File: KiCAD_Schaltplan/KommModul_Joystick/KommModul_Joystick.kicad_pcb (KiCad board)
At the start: 2 copper layers, 100 x 120 mm, 46 parts, among them J1 66100411622, J2 618015231121, J3 691242510004, J4 691242510004, J5 612020235121, J6 696106003002, SW1 430182080816, SW3 472123010111, U1 STM32F303RETx, U2 SP3485EN, U3 SP3485EN, U4 TLV1117LV33DCYR, Y1 16 MHz

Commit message: PCB Routing V1
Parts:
- moved J3 85.8 mm to (95.0, 129.5), turned to 180 degrees
- moved D5 82.8 mm to (113.0, 126.0), turned to 90 degrees
- moved J4 67.8 mm to (165.0, 129.5), turned to 180 degrees
- moved D6 65.5 mm to (147.5, 126.0), turned to 90 degrees
- moved J1 65.1 mm to (143.9, 39.0)
- moved C4 64.6 mm to (105.0, 110.5), turned to 90 degrees
- moved J5 56.3 mm to (175.5, 69.0), turned to 180 degrees
- moved C11 55.8 mm to (100.0, 82.5), turned to 180 degrees
- moved R8 48.1 mm to (101.8, 57.5)
- moved C1 47.4 mm to (85.5, 70.5)
- moved R5 47.2 mm to (160.0, 117.0)
- moved C3 45.5 mm to (93.5, 65.5)
- moved R4 44.8 mm to (100.4, 52.0), turned to -90 degrees
- moved R9 43.8 mm to (91.9, 57.0), turned to -90 degrees
- moved C5 43.7 mm to (164.9, 110.4), turned to 90 degrees
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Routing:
- net /VCC_3_3V: track 0.00 -> 177.8 mm, vias 0 -> 8
- net /VCC_5V: track 0.00 -> 57.7 mm, vias 0 -> 2
- net /UART_TX_Mtr_A: track 0.00 -> 46.3 mm, vias 0 -> 2
- net /UART_DE_Mtr_A: track 0.00 -> 43.1 mm
- net /UART_RX_Mtr_A: track 0.00 -> 42.7 mm
- net /UART_NRE_Mtr_A: track 0.00 -> 42.5 mm
- net /JS_X_axis: track 0.00 -> 41.8 mm, vias 0 -> 1
- net Net-(J3-Pad4): track 0.00 -> 41.1 mm
- net /UART_RX_Mtr_B: track 0.00 -> 39.7 mm
- net /UART_NRE_Mtr_B: track 0.00 -> 39.5 mm
- net /UART_DE_Mtr_B: track 0.00 -> 39.0 mm
- net /UART_TX_Mtr_B: track 0.00 -> 38.0 mm, vias 0 -> 2
- net /JS_Taster1: track 0.00 -> 36.6 mm, vias 0 -> 1
- net /JS_Y_axis: track 0.00 -> 33.5 mm, vias 0 -> 1
- net /JS_Taster2: track 0.00 -> 33.2 mm, vias 0 -> 1
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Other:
- board size 100 x 120 mm -> 100 x 100 mm

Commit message: change pcb v2
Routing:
- net /VCC_3_3V: track 177.8 -> 180.9 mm
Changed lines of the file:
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@@
+	)
+	(segment
+		(start 104.975 109.475)
+		(end 105 109.5)
+		(width 0.2)
+		(layer "F.Cu")
+		(net "/VCC_3_3V")
 	)
 	(segment
@@
 	)
 	(segment
+		(start 101.905 109.475)
+		(end 104.975 109.475)
+		(width 0.2)
+		(layer "F.Cu")
+		(net "/VCC_3_3V")
+	)
+	(segment
 		(start 140.426036 72.705051)
 		(end 135.719949 72.705051)
@@
 		(start 128 103.264312)
 		(end 125.764312 103.264312)
-		(width 0.2)
+		(width 0.5)
 		(layer "F.Cu")
 		(net "/VCC_5V")
@@
 		(start 100 89)
 		(end 100 82.5)
-		(width 0.2)
+		(width 0.5)
 		(layer "F.Cu")
 		(net "/VCC_5V")
@@
 		(start 137.5 114.5)
 		(end 131.2 108.2)
-		(width 0.2)
+		(width 0.5)
 		(layer "F.Cu")
 		(net "/VCC_5V")
@@
 		(start 131.2 103.3)
 		(end 128.035688 103.3)
-		(width 0.2)
+		(width 0.5)
 		(layer "F.Cu")
 		(net "/VCC_5V")
@@
 		(start 103.5 89)
 		(end 100 89)
-		(width 0.2)
+		(width 0.5)
 		(layer "F.Cu")
 		(net "/VCC_5V")
@@
 		(start 131.2 108.2)
 		(end 131.2 103.3)
-		(width 0.2)
+		(width 0.5)
 		(layer "F.Cu")
 		(net "/VCC_5V")
@@
 		(start 125.764312 103.264312)
 		(end 122.5 100)
-		(width 0.2)
+		(width 0.5)
 		(layer "F.Cu")
 		(net "/VCC_5V")
@@
 		(start 122.5 100)
 		(end 111.5 89)
-		(width 0.2)
+		(width 0.5)
 		(layer "B.Cu")
 		(net "/VCC_5V")
@@
 		(start 111.5 89)
 		(end 103.5 89)
-		(width 0.2)
+		(width 0.5)
 		(layer "B.Cu")
 		(net "/VCC_5V")
@@
 		(start 135 128.5)
 		(end 139.4 132.9)
-		(width 0.2)
+		(width 0.5)
 		(layer "F.Cu")
 		(net "Net-(J4-Pad4)")
@@
 		(start 147.5 132.9)
 		(end 153.98 132.9)
-		(width 0.2)
+		(width 0.5)
 		(layer "F.Cu")
 		(net "Net-(J4-Pad4)")
@@
 		(start 153.98 132.9)
 		(end 157.38 129.5)
-		(width 0.2)
+		(width 0.5)
 		(layer "F.Cu")
 		(net "Net-(J4-Pad4)")
@@
 		(start 139.4 132.9)
 		(end 147.5 132.9)
-		(width 0.2)
+		(width 0.5)
 		(layer "F.Cu")
 		(net "Net-(J4-Pad4)")
@@
 		(start 120.84 132.9)
 		(end 125.24 128.5)
-		(width 0.2)
+		(width 0.5)
 		(layer "F.Cu")
 		(net "Net-(J3-Pad4)")
@@
 		(start 87.38 129.5)
 		(end 90.78 132.9)
-		(width 0.2)
+		(width 0.5)
 		(layer "F.Cu")
 		(net "Net-(J3-Pad4)")
@@
 		(start 113 132.9)
 		(end 120.84 132.9)
-		(width 0.2)
+		(width 0.5)
 		(layer "F.Cu")
 		(net "Net-(J3-Pad4)")
@@
 		(start 90.78 132.9)
 		(end 113 132.9)
-		(width 0.2)
+		(width 0.5)
 		(layer "F.Cu")
 		(net "Net-(J3-Pad4)")
@@
 		(start 129.94 128.5)
 		(end 122.5 121.06)
-		(width 0.2)
+		(width 0.5)
 		(layer "F.Cu")
 		(net "Net-(J6-Pad1)")
@@
 		(start 122.5 121.06)
 		(end 122.5 114.5)
-		(width 0.2)
+		(width 0.5)
 		(layer "F.Cu")
 		(net "Net-(J6-Pad1)")

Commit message: PCB Layout V2
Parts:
- added C19: 100 nF, Capacitor_SMD_Wurth:C_Wurth_WCAP-CSGP-1206_H0.8, F.Cu at (154.0, 83.0)
- moved SW1 35.2 mm to (159.8, 77.5), turned to 90 degrees
- moved C5 6.09 mm to (166.0, 116.4)
- moved U2 6.00 mm to (100.0, 113.0)
- moved U3 6.00 mm to (160.0, 113.0)
- moved C4 5.57 mm to (105.5, 116.0)
- moved R2 3.50 mm to (100.0, 120.5)
- moved R5 3.00 mm to (160.0, 120.0)
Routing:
- net /NRST: track 0.00 -> 87.7 mm, vias 0 -> 4
- net /SWO: track 0.00 -> 52.3 mm
- net /SWCLK: track 0.00 -> 46.7 mm
- net /SWDIO: track 0.00 -> 45.6 mm, vias 0 -> 2
- net /Display_SCL: track 0.00 -> 41.0 mm
- net /VCC_5V: track 57.7 -> 98.6 mm, vias 2 -> 4
- net /Display_SDA: track 0.00 -> 40.2 mm
- net /JS_X_axis: track 41.8 -> 76.8 mm, vias 1 -> 2
- net /JS_Taster1: track 36.6 -> 70.8 mm, vias 1 -> 2
- net /JS_Y_axis: track 33.5 -> 67.1 mm, vias 1 -> 2
- net /JS_Z_axis: track 27.4 -> 60.6 mm, vias 1 -> 2
- net /JS_Taster2: track 33.2 -> 65.6 mm, vias 1 -> 2
- net /UART_NRE_Mtr_A: track 42.5 -> 54.5 mm
- net /VCC_3_3V: track 180.9 -> 189.4 mm
- net /UART_TX_Mtr_B: track 38.0 -> 45.5 mm
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
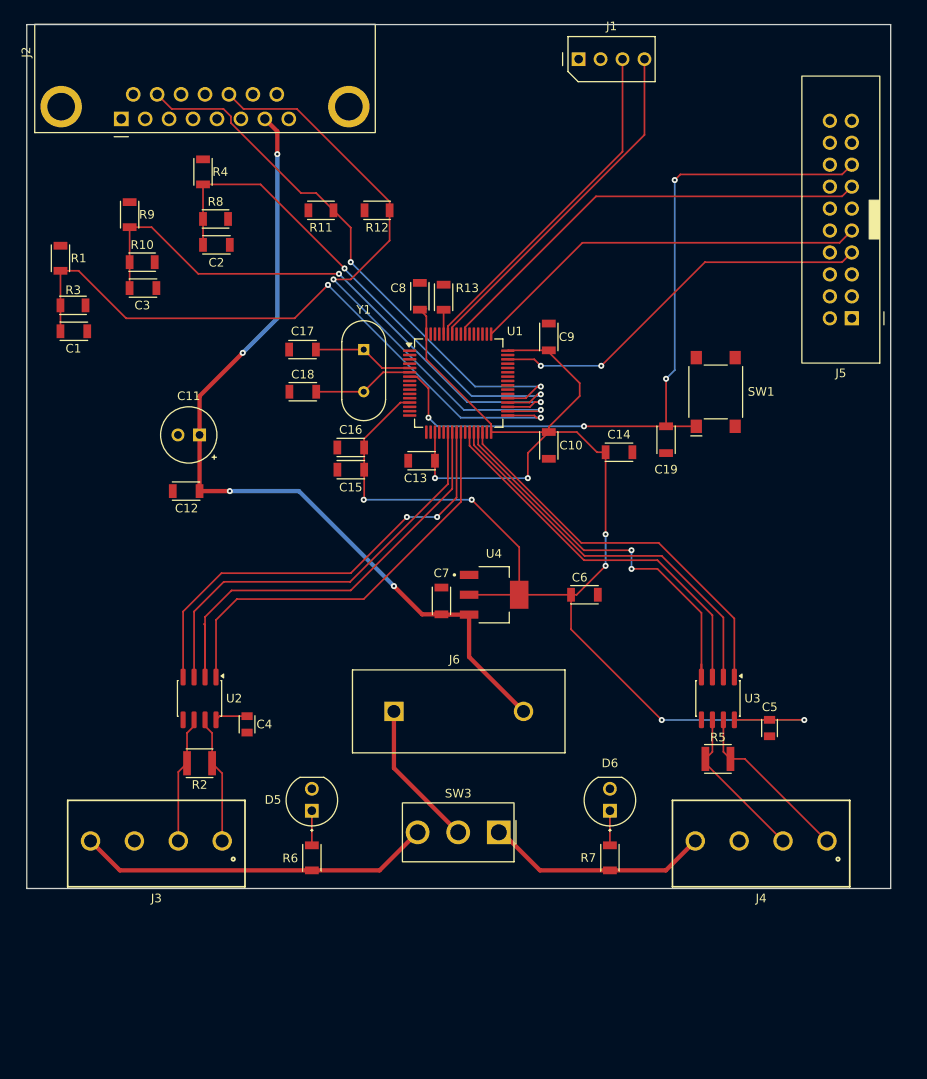
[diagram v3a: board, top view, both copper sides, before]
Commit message: Update PCB mit GND Plane
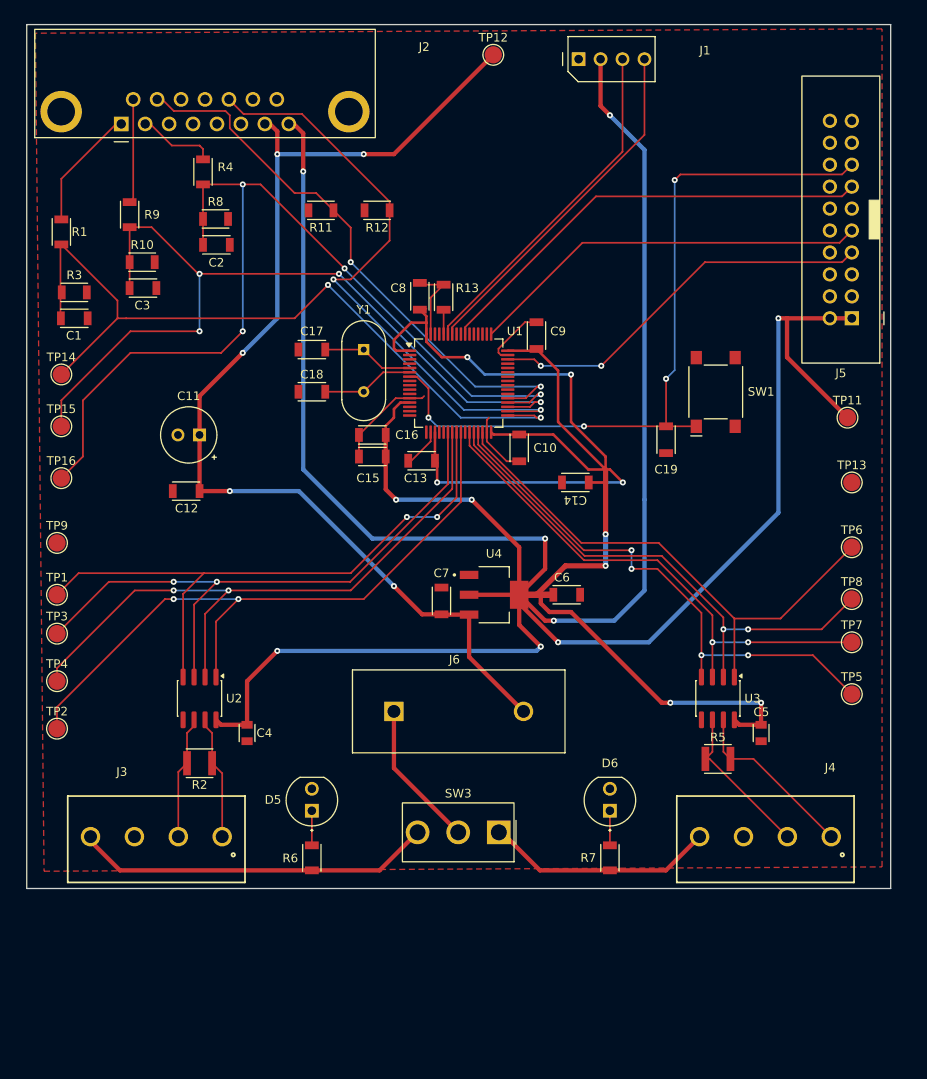
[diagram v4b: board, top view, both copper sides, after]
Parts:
- added TP1: TP_TX_A, TestPoint:TestPoint_Pad_D2.0mm, F.Cu at (83.5, 101.0)
- added TP11: TP_3_3V, TestPoint:TestPoint_Pad_D2.0mm, F.Cu at (175.0, 80.5)
- added TP12: TP_5V, TestPoint:TestPoint_Pad_D2.0mm, F.Cu at (134.0, 38.5)
- added TP13: TP_GND_2, TestPoint:TestPoint_Pad_D2.0mm, F.Cu at (175.5, 88.0)
- added TP14: TP_X_Axis, TestPoint:TestPoint_Pad_D2.0mm, F.Cu at (84.0, 75.5)
- added TP15: TP_Y_Axis, TestPoint:TestPoint_Pad_D2.0mm, F.Cu at (84.0, 81.5)
- added TP16: TP_Z_Axis, TestPoint:TestPoint_Pad_D2.0mm, F.Cu at (84.0, 87.5)
- added TP2: TP_RX_A, TestPoint:TestPoint_Pad_D2.0mm, F.Cu at (83.5, 116.5)
- added TP3: TP_DE_A, TestPoint:TestPoint_Pad_D2.0mm, F.Cu at (83.5, 105.5)
- added TP4: TP_NRE_A, TestPoint:TestPoint_Pad_D2.0mm, F.Cu at (83.5, 111.0)
- added TP5: TP_TX_B, TestPoint:TestPoint_Pad_D2.0mm, F.Cu at (175.5, 112.5)
- added TP6: TP_RX_B, TestPoint:TestPoint_Pad_D2.0mm, F.Cu at (175.5, 95.5)
- added TP7: TP_DE_B, TestPoint:TestPoint_Pad_D2.0mm, F.Cu at (175.5, 106.5)
- added TP8: TP_NRE_B, TestPoint:TestPoint_Pad_D2.0mm, F.Cu at (175.5, 101.5)
- added TP9: TP_GND_1, TestPoint:TestPoint_Pad_D2.0mm, F.Cu at (83.5, 95.0)
- moved C14 6.14 mm to (143.5, 88.0), turned to 180 degrees
- moved C10 3.44 mm to (137.0, 84.0)
- moved R1 3.05 mm to (84.0, 59.0)
- moved C15 2.92 mm to (120.0, 85.0)
- moved C16 2.89 mm to (120.0, 82.5)
- moved C6 2.05 mm to (142.5, 101.0)
- moved R3 1.51 mm to (85.5, 66.0)
- moved C1 1.50 mm to (85.5, 69.0)
- moved C9 1.43 mm to (139.0, 71.0)
- moved C5 1.13 mm to (165.0, 117.0)
- moved C17 1.08 mm to (113.0, 72.6)
- moved C18 1.05 mm to (113.0, 77.5)
- moved C4 1.00 mm to (105.5, 117.0)
- moved J4 0.71 mm to (165.5, 129.0)
- moved J2 0.58 mm to (90.9, 46.5)
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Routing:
- net /VCC_3_3V: track 189.4 -> 510.2 mm, vias 8 -> 18
- net /JS_Z_axis: track 60.6 -> 109.4 mm, vias 2 -> 4
- net GND: track 0.00 -> 40.6 mm
- net /VCC_5V: track 98.6 -> 127.8 mm, vias 4 -> 5
- net /JS_Y_axis: track 67.1 -> 96.1 mm, vias 2 -> 4
- net /UART_RX_Mtr_A: track 48.7 -> 77.3 mm, vias 0 -> 2
- net /UART_DE_Mtr_A: track 49.1 -> 70.5 mm, vias 0 -> 2
- net /UART_TX_Mtr_A: track 52.3 -> 71.5 mm
- net /UART_NRE_Mtr_A: track 54.5 -> 73.6 mm, vias 0 -> 2
- net /UART_TX_Mtr_B: track 45.5 -> 63.3 mm, vias 2 -> 4
- net /UART_RX_Mtr_B: track 45.7 -> 62.7 mm
- net /UART_NRE_Mtr_B: track 45.5 -> 61.9 mm, vias 0 -> 2
- net /UART_DE_Mtr_B: track 45.0 -> 61.1 mm, vias 0 -> 2
- net Net-(J2-Pad1): track 0.00 -> 14.4 mm
- net /JS_X_axis: track 76.8 -> 90.1 mm
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- added copper zone on F.Cu, net GND

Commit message: PCB Layout Change
Ueberarbeitung des Routing, hinzufuegen von GND Zonen
Bohrungen fehlen noch
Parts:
- moved SW1 7.24 mm to (156.5, 84.0), turned to 0 degrees
- moved C19 5.00 mm to (149.0, 83.0)
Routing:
- net GND: track 40.6 -> 172.7 mm, vias 0 -> 45
- net /NRST: track 87.7 -> 84.9 mm
- net /VCC_3_3V: track 510.2 -> 512.0 mm
- net /JS_Taster1: track 71.1 -> 71.8 mm
- net /JS_Taster2: track 65.8 -> 65.2 mm
- added copper zone on F.Cu, net /VCC_3_3V
- added copper zone on B.Cu, net GND

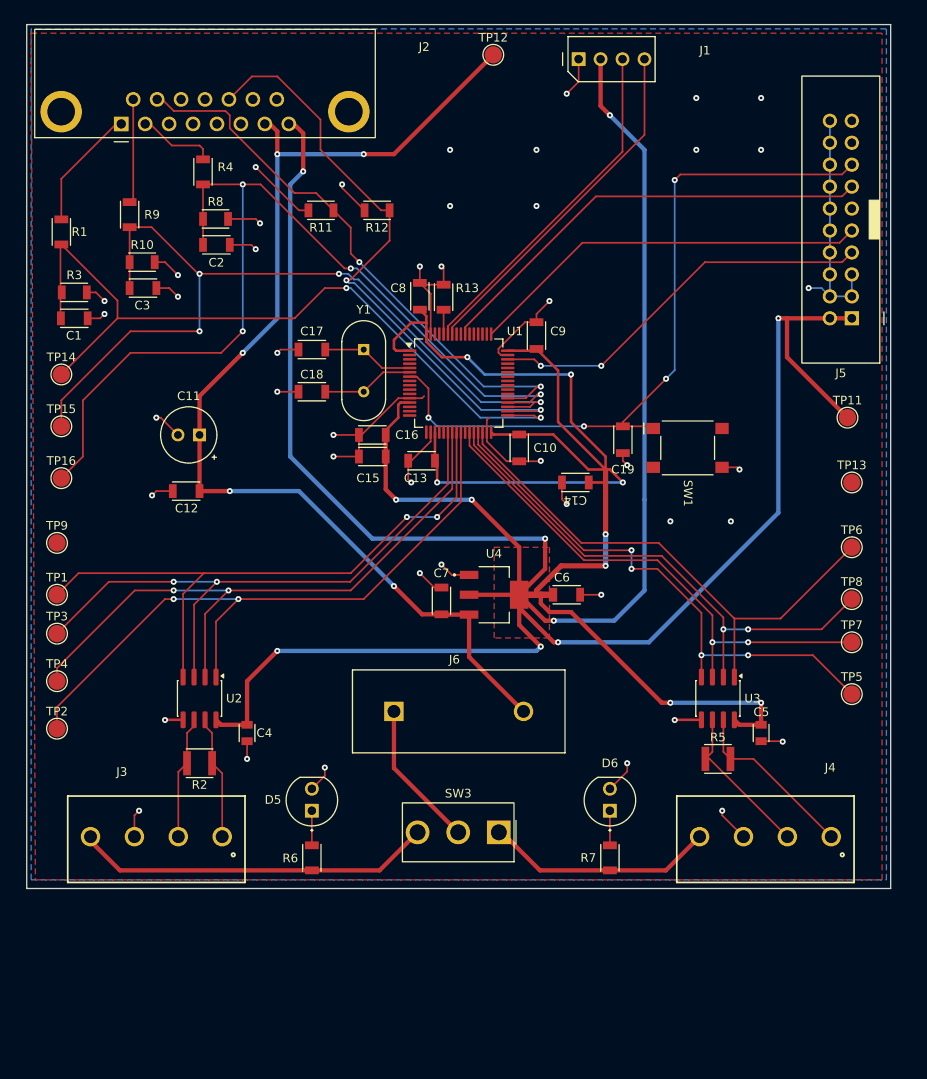
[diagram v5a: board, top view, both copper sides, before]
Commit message: Final Changes
Finale Aenderung am PCB Erzeugung der Drill und Gerber Files
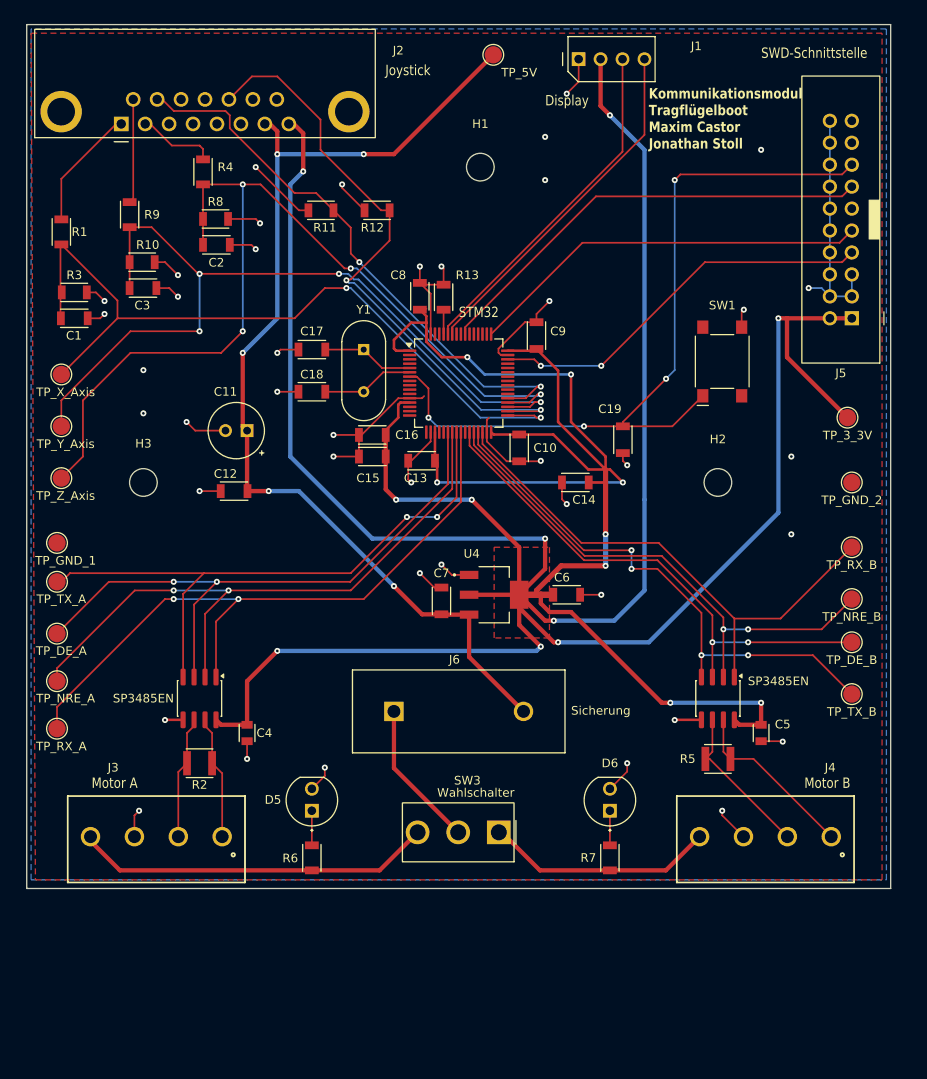
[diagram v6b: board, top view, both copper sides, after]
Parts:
- added H1: MountingHole, MountingHole:MountingHole_3.2mm_M3, F.Cu at (132.5, 51.5)
- added H2: MountingHole, MountingHole:MountingHole_3.2mm_M3, F.Cu at (160.0, 88.0)
- added H3: MountingHole, MountingHole:MountingHole_3.2mm_M3, F.Cu at (93.5, 88.0)
- moved SW1 10.8 mm to (160.5, 74.0), turned to 90 degrees
- moved C12 5.55 mm to (104.0, 89.0)
- moved C11 5.52 mm to (105.5, 82.0)
- moved TP1 1.50 mm to (83.5, 99.5)
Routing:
- net /VCC_5V: track 127.8 -> 120.4 mm
- net /NRST: track 84.9 -> 92.0 mm
- net GND: track 172.7 -> 174.1 mm, vias 45 -> 42
- net /UART_TX_Mtr_A: track 71.5 -> 70.9 mm
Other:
- board text added: "Display"
- board text added: "Joystick"
- board text added: "Kommunikationsmodul Tragflügelboot Maxim Castor Jonathan Stoll"
- board text added: "Motor A"
- board text added: "Motor B"
- board text added: "STM32"
- board text added: "SWD-Schnittstelle"
- board text added: "Sicherung"
- board text added: "Wahlschalter"
